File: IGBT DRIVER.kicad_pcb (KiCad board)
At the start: 2 copper layers, 145 x 70 mm, 123 parts, among them J1 Conn_01x04, J2 Conn_01x04, J3 Conn_01x01, J4 Conn_01x04, J5 Conn_02x05_Odd_Even, J6 Conn_01x02_Male, Q1 MMBT5551L, Q2 MMBT5551L, Q3 MMBT5551L, Q4 MMBT5401, Q5 MMBT5551L, Q6 MMBT5551L, Q7 MMBT5551L, Q8 MMBT5551L, U1 miw06-24s24, U2 EXB841, U3 PC817, U4 SN75452BP, U5 AMS1117-5.0, U6 PC817, U7 PC817

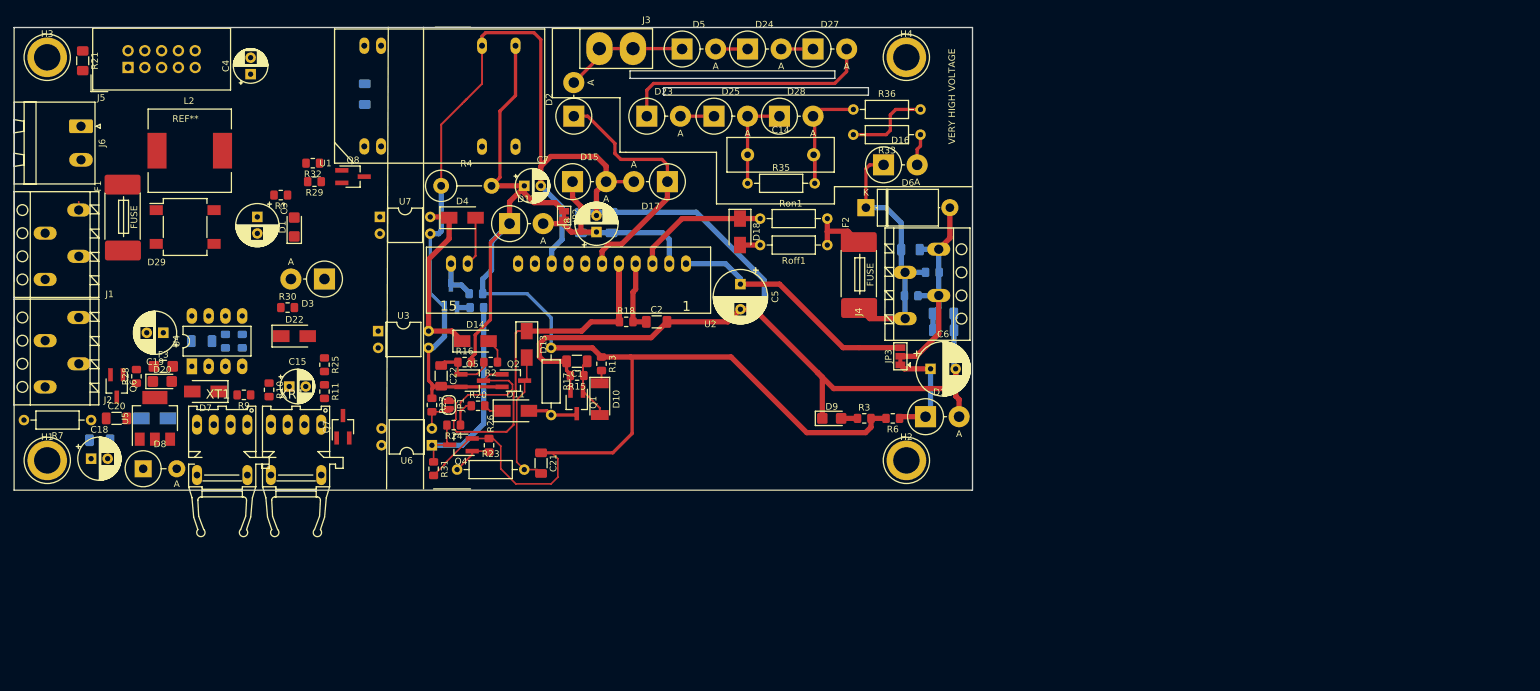
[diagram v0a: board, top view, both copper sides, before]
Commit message: skm200 layout added
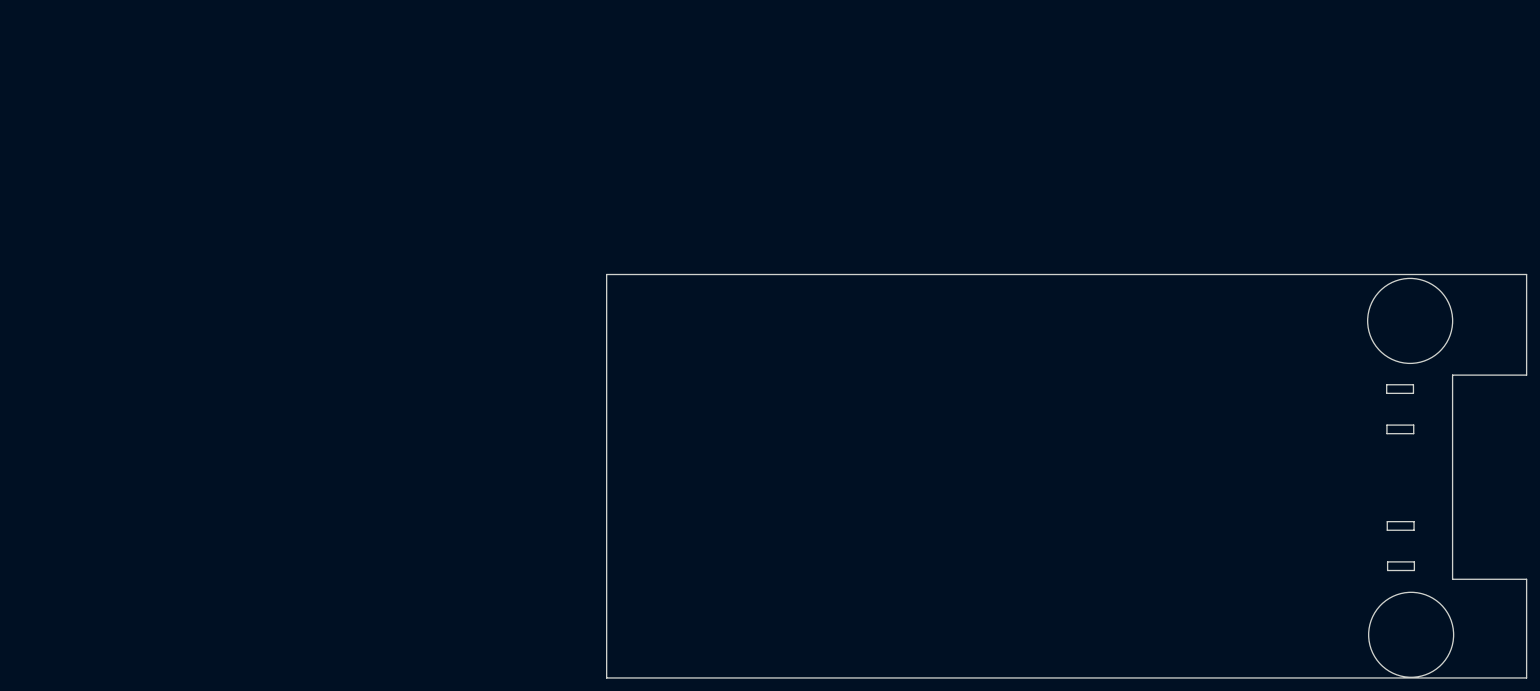
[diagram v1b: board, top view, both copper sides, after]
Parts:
- removed C1: 1nF, Capacitor_SMD:C_1206_3216Metric_Pad1.33x1.80mm_HandSolder
- removed C10, C11: 1uF, Capacitor_SMD:C_1206_3216Metric_Pad1.33x1.80mm_HandSolder
- removed C12, C13, C16, C17, C20: 100nF, Capacitor_SMD:C_1206_3216Metric_Pad1.33x1.80mm_HandSolder
- removed C14: 100nF, Capacitor_THT:C_Disc_D16.0mm_W5.0mm_P10.00mm
- removed C15: 4.7uf/16v, Capacitor_THT:CP_Radial_D5.0mm_P2.50mm
- removed C18, C19, C3, C8: 100uf/35v, Capacitor_THT:CP_Radial_D6.3mm_P2.50mm
- removed C2: C, Capacitor_SMD:C_1206_3216Metric_Pad1.33x1.80mm_HandSolder
- removed C21: 100pF, Capacitor_SMD:C_1206_3216Metric_Pad1.33x1.80mm_HandSolder
- removed C22: 10uF, Capacitor_SMD:C_1206_3216Metric_Pad1.33x1.80mm_HandSolder
- removed C4, C7: 10uf/35v, Capacitor_THT:CP_Radial_D5.0mm_P2.50mm
- removed C5, C6: 47uf/35v, Capacitor_THT:CP_Radial_D8.0mm_P3.80mm
- removed C9: 100nf, Capacitor_SMD:C_1206_3216Metric_Pad1.33x1.80mm_HandSolder
- removed Cclamp1: C, Capacitor_SMD:C_1206_3216Metric
- removed D1, D20, D9: LED, LED_SMD:LED_1206_3216Metric_Castellated
- removed D10: BZX85C20, Diode_SMD:D_MELF
- removed D11, D13, D14, D18, D21, D22, D4: SS14, Diode_SMD:D_SMA
- removed D12, D3: 1.5KE4A, Diode_THT:D_DO-201AD_P5.08mm_Vertical_AnodeUp
- removed D15: 1.5KE24A, Diode_THT:D_DO-201AD_P5.08mm_Vertical_AnodeUp
- removed D16: 1.5KE7A, Diode_THT:D_DO-201AD_P5.08mm_Vertical_AnodeUp
- removed D17: 1.5KE13A, Diode_THT:D_DO-201AD_P5.08mm_Vertical_AnodeUp
- removed D19: 1.5KE8A, Diode_THT:D_DO-201AD_P5.08mm_Vertical_AnodeUp
- removed D2: BYV26E, Diode_THT:D_DO-201AD_P5.08mm_Vertical_AnodeUp
- removed D23, D24, D25, D27, D28, D5: 1.5KE160A, Diode_THT:D_DO-201AD_P5.08mm_Vertical_AnodeUp
- removed D29: DF10M, Diode_SMD:Diode_Bridge_Vishay_DFS
- removed D6: 1.5KE16CA, Diode_THT:D_DO-201AE_P12.70mm_Horizontal
- removed D7: 1N4001, Diode_SMD:D_SMA
- removed D8: 1N5338B, Diode_THT:D_DO-201_P5.08mm_Vertical_AnodeUp
- removed F1, F2: Fuse_Small, gh- kicad:fuse.holder.1808
- removed F3: 0.5A, Fuse:Fuse_1206_3216Metric_Castellated
- removed H1, H2, H3, H4: MountingHole, TestPoint:TestPoint_Plated_Hole_D4.0mm
- removed J1, J2, J4: Conn_01x04, gh- kicad:WJ250-3.5
- removed J3: Conn_01x01, gh- kicad:COOLERI
- removed J5: Conn_02x05_Odd_Even, Connector_IDC:IDC-Header_2x05_P2.54mm_Vertical
- removed J6: Conn_01x02_Male, Connector_Phoenix_MSTB:PhoenixContact_MSTBA_2,5_2-G-5,08_1x02_P5.08mm_Horizontal
- removed JP1: SolderJumper_2_Open, Jumper:SolderJumper-2_P1.3mm_Open_RoundedPad1.0x1.5mm
- removed JP2: SolderJumper_2_Bridged, Jumper:SolderJumper-2_P1.3mm_Bridged_Pad1.0x1.5mm
- removed JP3: SolderJumper_3_Bridged12, Jumper:SolderJumper-3_P1.3mm_Bridged12_Pad1.0x1.5mm
- removed L2: 10uh, gh- kicad:INDUCTOR.SMD.12
- removed Q1, Q2, Q3, Q5, Q6, Q7, Q8: MMBT5551L, Package_TO_SOT_SMD:SOT-23W_Handsoldering
- removed Q4: MMBT5401, Package_TO_SOT_SMD:SOT-23W_Handsoldering
- removed R1, R19, R3: 1.8k, Resistor_SMD:R_0805_2012Metric_Pad1.15x1.40mm_HandSolder
- removed R10, R11: 2.7k, Resistor_SMD:R_0805_2012Metric_Pad1.15x1.40mm_HandSolder
- removed R12, R14, R22, R25, R29, R30, R32, R9: 1k, Resistor_SMD:R_0805_2012Metric_Pad1.15x1.40mm_HandSolder
- removed R13, R15: 1K, Resistor_SMD:R_0805_2012Metric_Pad1.15x1.40mm_HandSolder
- removed R16, R2: r, Resistor_SMD:R_0805_2012Metric_Pad1.15x1.40mm_HandSolder
- removed R17, R23: 3.3k-1/4W, Resistor_THT:R_Axial_DIN0207_L6.3mm_D2.5mm_P10.16mm_Horizontal
- removed R18: R, Resistor_SMD:R_0805_2012Metric_Pad1.15x1.40mm_HandSolder
- removed R20: 500R, Resistor_SMD:R_0805_2012Metric_Pad1.15x1.40mm_HandSolder
- removed R21: 10/0.25W, Resistor_SMD:R_1206_3216Metric_Pad1.42x1.75mm_HandSolder
- removed R24, R26, R27: 3.3K, Resistor_SMD:R_0805_2012Metric_Pad1.15x1.40mm_HandSolder
- removed R28: 10K, Resistor_SMD:R_0805_2012Metric_Pad1.15x1.40mm_HandSolder
- removed R31: not mount, Resistor_SMD:R_0805_2012Metric_Pad1.15x1.40mm_HandSolder
- removed R33: 100, Resistor_THT:R_Axial_DIN0207_L6.3mm_D2.5mm_P10.16mm_Horizontal
- removed R34, R8: 20K, Resistor_SMD:R_0805_2012Metric_Pad1.15x1.40mm_HandSolder
- removed R35: 20K, Resistor_THT:R_Axial_DIN0207_L6.3mm_D2.5mm_P10.16mm_Horizontal
- removed R36: 120, Resistor_THT:R_Axial_DIN0207_L6.3mm_D2.5mm_P10.16mm_Horizontal
- removed R4: 2k/1w, Resistor_THT:R_Axial_DIN0414_L11.9mm_D4.5mm_P7.62mm_Vertical
- removed R5: 3k, Resistor_SMD:R_0805_2012Metric_Pad1.15x1.40mm_HandSolder
- removed R6: 6.8k, Resistor_SMD:R_0805_2012Metric_Pad1.15x1.40mm_HandSolder
- removed R7: 10/0.25W, Resistor_THT:R_Axial_DIN0207_L6.3mm_D2.5mm_P10.16mm_Horizontal
- removed Roff1, Ron1: 20, Resistor_THT:R_Axial_DIN0207_L6.3mm_D2.5mm_P10.16mm_Horizontal
- removed U1: miw06-24s24, gh- kicad:MIWI06
- removed U2: EXB841, gh- kicad:EXB841
- removed U3, U6, U7: PC817, Package_DIP:DIP-4_W7.62mm
- removed U4: SN75452BP, Package_DIP:DIP-8_W7.62mm_LongPads
- removed U5: AMS1117-5.0, Package_TO_SOT_SMD:SOT-223-3_TabPin2
- removed XR1: HFBR-2521, gh- kicad:HFBR-15X3
- removed XT1: HFBR-1521, KIcad:HFBR-15X3
- added G***: LOGO, IGBT-DRIVER-emad:skm200GB, F.Cu at (342.3, 121.9)
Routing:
- net GNDPWR: track 296.7 -> 0.00 mm
- net +24V: track 211.1 -> 0.00 mm
- net /Fault: track 62.9 -> 0.00 mm
- net VPP: track 44.2 -> 0.00 mm
- net /GATE: track 40.6 -> 0.00 mm
- net Net-(D23-Pad1): track 38.7 -> 0.00 mm
- net /EMITTER: track 38.7 -> 0.00 mm
- net Net-(D17-Pad1): track 38.3 -> 0.00 mm
- net Net-(C5-Pad1): track 38.2 -> 0.00 mm
- net /lockpwm: track 35.3 -> 0.00 mm
- net /Latchreset: track 27.1 -> 0.00 mm
- net Net-(Q2-Pad1): track 24.7 -> 0.00 mm
- net Net-(C14-Pad2): track 21.2 -> 0.00 mm
- net Net-(C21-Pad2): track 20.8 -> 0.00 mm
- net Net-(D18-Pad1): track 20.5 -> 0.00 mm
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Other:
- board size 145 x 70 mm -> 139.2 x 61 mm
- board text removed: "VERY HIGH VOLTAGE"

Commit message: skm200 3d
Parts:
- removed G***: LOGO, IGBT-DRIVER-emad:skm200GB
- added C1: 100nF, Capacitor_SMD:C_1206_3216Metric_Pad1.33x1.80mm_HandSolder, F.Cu at (315.7, 39.5)
- added C10: 47uf/35v, Capacitor_THT:CP_Radial_D8.0mm_P3.80mm, F.Cu at (332.2, 69.8)
- added C11: 1uF, Capacitor_SMD:C_1206_3216Metric_Pad1.33x1.80mm_HandSolder, F.Cu at (396.3, 3.49)
- added C12: 100nF, Capacitor_THT:C_Disc_D16.0mm_W5.0mm_P10.00mm, F.Cu at (277.2, 48.0)
- added C13: 100nF, Capacitor_SMD:C_1206_3216Metric_Pad1.33x1.80mm_HandSolder, F.Cu at (396.3, 6.84)
- added C14: 10nF, Capacitor_SMD:C_1206_3216Metric_Pad1.33x1.80mm_HandSolder, F.Cu at (327.5, 84.5)
- added C15: 1nF, Capacitor_SMD:C_1206_3216Metric_Pad1.33x1.80mm_HandSolder, F.Cu at (341.9, 67.8)
- added C16: 10uf/35v, Capacitor_THT:CP_Radial_D5.0mm_P2.50mm, F.Cu at (388.8, 5.59)
- added C17: 100nf, Capacitor_SMD:C_1206_3216Metric_Pad1.33x1.80mm_HandSolder, F.Cu at (389.8, 13.9)
- added C18: 10uf/35v, Capacitor_THT:CP_Radial_D5.0mm_P2.50mm, F.Cu at (393.1, -1.46)
- added C19: 1uF, Capacitor_SMD:C_1206_3216Metric_Pad1.33x1.80mm_HandSolder, F.Cu at (383.7, 17.2)
- added C2: 47uf/35v, Capacitor_THT:CP_Radial_D8.0mm_P3.80mm, F.Cu at (332.2, 20.3)
- added C20: 100nF, Capacitor_SMD:C_1206_3216Metric_Pad1.33x1.80mm_HandSolder, F.Cu at (383.1, 21.3)
- added C21: 47uf/35v, Capacitor_THT:CP_Radial_D8.0mm_P3.80mm, F.Cu at (322.3, 28.5)
- added C22: 100nF, Capacitor_SMD:C_1206_3216Metric_Pad1.33x1.80mm_HandSolder, F.Cu at (327.5, 35.0)
- added C23: 47uf/35v, Capacitor_THT:CP_Radial_D8.0mm_P3.80mm, F.Cu at (322.3, 78.0)
- added C24: 100nF, Capacitor_SMD:C_1206_3216Metric_Pad1.33x1.80mm_HandSolder, F.Cu at (303.7, 88.6)
- added C3: 100uf/35v, Capacitor_THT:CP_Radial_D6.3mm_P2.50mm, F.Cu at (361.9, 11.3)
- added C4: 10uf/35v, Capacitor_THT:CP_Radial_D5.0mm_P2.50mm, F.Cu at (376.2, 16.3)
- added C5: 1nF, Capacitor_SMD:C_1206_3216Metric_Pad1.33x1.80mm_HandSolder, F.Cu at (341.9, 15.0)
- added C6: 100nF, Capacitor_SMD:C_1206_3216Metric_Pad1.33x1.80mm_HandSolder, F.Cu at (346.1, 61.1)
- added C7: 10uf/35v, Capacitor_THT:CP_Radial_D5.0mm_P2.50mm, F.Cu at (399.8, -1.46)
- added C8: 100uf/35v, Capacitor_THT:CP_Radial_D6.3mm_P2.50mm, F.Cu at (374.5, 9.14)
- added C9: 100nf, Capacitor_SMD:C_1206_3216Metric_Pad1.33x1.80mm_HandSolder, F.Cu at (389.7, 10.5)
- added CDynamic1: 100nF, Capacitor_THT:C_Disc_D16.0mm_W5.0mm_P10.00mm, F.Cu at (277.2, -1.46)
- added CShortPulseFilter1: 100pF, Capacitor_SMD:C_1206_3216Metric_Pad1.33x1.80mm_HandSolder, F.Cu at (303.7, 39.1)
- added CblankTime1: 100pF, Capacitor_SMD:C_1206_3216Metric_Pad1.33x1.80mm_HandSolder, F.Cu at (346.1, 11.6)
- added Cclamp1: C, Capacitor_SMD:C_1206_3216Metric, F.Cu at (316.0, 14.5)
- added Cclamp2: C, Capacitor_SMD:C_1206_3216Metric, F.Cu at (316.0, 64.0)
- added Cex1: 96pF, Capacitor_SMD:C_1206_3216Metric_Pad1.33x1.80mm_HandSolder, F.Cu at (309.7, 39.1)
- added Cex2: 1nF, Capacitor_SMD:C_1206_3216Metric_Pad1.33x1.80mm_HandSolder, F.Cu at (348.9, 8.24)
- added Cex3: 96pF, Capacitor_SMD:C_1206_3216Metric_Pad1.33x1.80mm_HandSolder, F.Cu at (309.7, 88.6)
- added Cex4: 100pF, Capacitor_SMD:C_1206_3216Metric_Pad1.33x1.80mm_HandSolder, F.Cu at (315.7, 89.0)
- added Cex5: 100pF, Capacitor_SMD:C_1206_3216Metric_Pad1.33x1.80mm_HandSolder, F.Cu at (341.9, 64.5)
- added Cex6: 1nF, Capacitor_SMD:C_1206_3216Metric_Pad1.33x1.80mm_HandSolder, F.Cu at (332.0, 76.2)
- added Cex7: 22nF, Capacitor_SMD:C_1206_3216Metric_Pad1.33x1.80mm_HandSolder, F.Cu at (348.9, 57.7)
- added CsoftTurnOff2: 10nF, Capacitor_SMD:C_1206_3216Metric_Pad1.33x1.80mm_HandSolder, F.Cu at (332.0, 26.7)
- added CsoftTurnOffTiming1: 22nF, Capacitor_SMD:C_1206_3216Metric_Pad1.33x1.80mm_HandSolder, F.Cu at (341.9, 18.3)
- added D1: LED, LED_SMD:LED_1206_3216Metric_Castellated, F.Cu at (383.8, 13.9)
- added D10: Dz8v, Diode_THT:D_DO-201AD_P5.08mm_Vertical_AnodeUp, F.Cu at (311.8, 78.8)
- added D11: 1.5KE13A, Diode_THT:D_DO-201AD_P5.08mm_Vertical_AnodeUp, F.Cu at (345.1, 48.1)
- added D12: 1.5KE6V8A, Diode_THT:D_DO-201AD_P5.08mm_Vertical_AnodeUp, F.Cu at (327.6, 61.6)
- added D13: BYV26E, Diode_THT:D_DO-201AD_P5.08mm_Vertical_AnodeUp, F.Cu at (290.1, 83.5)
- added D14: Dz10v, Diode_THT:D_DO-201AD_P5.08mm_Vertical_AnodeUp, F.Cu at (311.8, 72.0)
- added D15: 26v TVS, Diode_SMD:D_MELF, F.Cu at (296.8, 89.1)
- added D16: 1.5KE160A, Diode_THT:D_DO-201AD_P5.08mm_Vertical_AnodeUp, F.Cu at (327.6, 54.9)
- added D17: 1.5KE160A, Diode_THT:D_DO-201AD_P5.08mm_Vertical_AnodeUp, F.Cu at (301.0, 76.8)
- added D18: 1.5KE160A, Diode_THT:D_DO-201AD_P5.08mm_Vertical_AnodeUp, F.Cu at (338.4, 54.9)
- added D19: 1.5KE160A, Diode_THT:D_DO-201AD_P5.08mm_Vertical_AnodeUp, F.Cu at (301.0, 83.6)
- added D2: 1.5KE4A, Diode_THT:D_DO-201AD_P5.08mm_Vertical_AnodeUp, F.Cu at (338.4, 5.39)
- added D20: 1.5KE160A, Diode_THT:D_DO-201AD_P5.08mm_Vertical_AnodeUp, F.Cu at (316.7, 52.2)
- added D21: 1.5KE160A, Diode_THT:D_DO-201AD_P5.08mm_Vertical_AnodeUp, F.Cu at (334.3, 48.1)
- added D22: BZX85C20, Diode_SMD:D_MELF, F.Cu at (288.9, 89.0)
- added D29: DF10M, Diode_SMD:Diode_Bridge_Vishay_DFS, F.Cu at (377.8, 0.24)
- added D3: Dz8v, Diode_THT:D_DO-201AD_P5.08mm_Vertical_AnodeUp, F.Cu at (316.7, 2.69)
- added D4: 1.5KE13A, Diode_THT:D_DO-201AD_P5.08mm_Vertical_AnodeUp, F.Cu at (301.0, 27.3)
- added D5: BYV26E, Diode_THT:D_DO-201AD_P5.08mm_Vertical_AnodeUp, F.Cu at (316.7, 9.44)
- added D6: 1.5KE6V8A, Diode_THT:D_DO-201AD_P5.08mm_Vertical_AnodeUp, F.Cu at (334.3, -1.36)
- added D7: 26v TVS, Diode_SMD:D_MELF, F.Cu at (296.8, 39.6)
- added D8: 1.5KE4A, Diode_THT:D_DO-201AD_P5.08mm_Vertical_AnodeUp, F.Cu at (316.7, 58.9)
- added D9: LED, LED_SMD:LED_1206_3216Metric_Castellated, F.Cu at (377.1, 21.3)
- added DStatic1: 1.5KE160A, Diode_THT:D_DO-201AD_P5.08mm_Vertical_AnodeUp, F.Cu at (327.6, 5.39)
- added DStatic2: 1.5KE160A, Diode_THT:D_DO-201AD_P5.08mm_Vertical_AnodeUp, F.Cu at (311.8, 22.5)
- added DStatic3: 1.5KE160A, Diode_THT:D_DO-201AD_P5.08mm_Vertical_AnodeUp, F.Cu at (301.0, 34.1)
- added DStatic4: 1.5KE160A, Diode_THT:D_DO-201AD_P5.08mm_Vertical_AnodeUp, F.Cu at (290.1, 34.0)
- added DStatic5: 1.5KE160A, Diode_THT:D_DO-201AD_P5.08mm_Vertical_AnodeUp, F.Cu at (345.1, -1.36)
- added DZunderVoltageFault1: BZX85C20, Diode_SMD:D_MELF, F.Cu at (288.9, 39.5)
- added Dex1: 1n4148, Diode_SMD:D_SMA, F.Cu at (339.1, 11.0)
- added Dex10: 1n4148, Diode_SMD:D_SMA, F.Cu at (312.4, 84.4)
- added Dex2: 1n4148, Diode_SMD:D_SMA, F.Cu at (312.4, 34.9)
- added Dex3: 1n4148, Diode_SMD:D_SMA, F.Cu at (320.5, 85.1)
- added Dex4: 1n4148, Diode_SMD:D_SMA, F.Cu at (302.3, 70.9)
- added Dex5: 1n4148, Diode_SMD:D_SMA, F.Cu at (320.5, 35.6)
- added Dex6: 1n4148, Diode_SMD:D_SMA, F.Cu at (349.9, 53.8)
- added Dex7: 1n4148, Diode_SMD:D_SMA, F.Cu at (339.1, 60.5)
- added DprotectionHigh1: 1n4148, Diode_SMD:D_SMA, F.Cu at (302.3, 21.4)
- added DprotectionLow1: 1n4148, Diode_SMD:D_SMA, F.Cu at (349.9, 4.29)
- added DzDynamic1: 1.5KE160A, Diode_THT:D_DO-201AD_P5.08mm_Vertical_AnodeUp, F.Cu at (311.8, 29.3)
- added DzSaturation1: Dz10v, Diode_THT:D_DO-201AD_P5.08mm_Vertical_AnodeUp, F.Cu at (327.6, 12.1)
- added H1: MountingHole, TestPoint:TestPoint_Plated_Hole_D4.0mm, F.Cu at (370.6, 16.6)
- added H2: MountingHole, TestPoint:TestPoint_Plated_Hole_D4.0mm, F.Cu at (362.6, 18.7)
- added H3: MountingHole, TestPoint:TestPoint_Plated_Hole_D4.0mm, F.Cu at (383.2, 8.74)
- added H4: MountingHole, TestPoint:TestPoint_Plated_Hole_D4.0mm, F.Cu at (387.5, -1.21)
- added Q1: BC817, Package_TO_SOT_SMD:SOT-23, F.Cu at (351.5, 12.2)
- added Q10: BC817, Package_TO_SOT_SMD:SOT-23, F.Cu at (337.2, 81.4)
- added Q11: BC817, Package_TO_SOT_SMD:SOT-23, F.Cu at (351.5, 61.7)
- added Q12: BC817, Package_TO_SOT_SMD:SOT-23, F.Cu at (345.5, 71.8)
- added Q13: BC817, Package_TO_SOT_SMD:SOT-23, F.Cu at (332.7, 84.7)
- added Q14: BC807, Package_TO_SOT_SMD:SOT-23, F.Cu at (326.7, 88.4)
- added Q15: BC817, Package_TO_SOT_SMD:SOT-23, F.Cu at (341.1, 71.8)
- added Q16: BC817, Package_TO_SOT_SMD:SOT-23, F.Cu at (337.2, 76.8)
- added Q17: BC807, Package_TO_SOT_SMD:SOT-23, F.Cu at (347.1, 65.0)
- added Q18: BC817, Package_TO_SOT_SMD:SOT-23, F.Cu at (331.2, 80.2)
- added Q19: TIP41, Package_TO_SOT_THT:TO-220-3_Vertical, F.Cu at (290.0, 71.4)
- added Q2: BC817, Package_TO_SOT_SMD:SOT-23, F.Cu at (345.5, 22.3)
- added Q20: TIP42, Package_TO_SOT_THT:TO-220-3_Vertical, F.Cu at (276.7, 87.6)
- added Q3: BC817, Package_TO_SOT_SMD:SOT-23, F.Cu at (337.2, 31.9)
- added Q4: BC807, Package_TO_SOT_SMD:SOT-23, F.Cu at (332.7, 35.2)
- added Q5: BC817, Package_TO_SOT_SMD:SOT-23, F.Cu at (326.7, 38.9)
- added Q6: BC817, Package_TO_SOT_SMD:SOT-23, F.Cu at (341.1, 22.3)
- added Q7: BC817, Package_TO_SOT_SMD:SOT-23, F.Cu at (337.2, 27.3)
- added Q8: TIP41, Package_TO_SOT_THT:TO-220-3_Vertical, F.Cu at (276.7, 38.1)
- added Q9: TIP42, Package_TO_SOT_THT:TO-220-3_Vertical, F.Cu at (290.0, 21.9)
- added Qclamp1: BUK7880-55A, Package_TO_SOT_SMD:SOT-223-3_TabPin2, F.Cu at (324.2, 19.6)
- added Qclamp2: BUK7880-55A, Package_TO_SOT_SMD:SOT-223-3_TabPin2, F.Cu at (324.2, 69.1)
- added QfaultLatch1: BC807, Package_TO_SOT_SMD:SOT-23, F.Cu at (331.2, 30.7)
- added QsoftTurnOnn1: BC817, Package_TO_SOT_SMD:SOT-23, F.Cu at (347.1, 15.5)
- added R10: 2k/1w, Resistor_THT:R_Axial_DIN0414_L11.9mm_D4.5mm_P7.62mm_Vertical, F.Cu at (362.1, -1.71)
- added R14: 20K, Resistor_THT:R_Axial_DIN0207_L6.3mm_D2.5mm_P10.16mm_Horizontal, F.Cu at (301.6, 54.9)
- added R15: 10, Resistor_THT:R_Axial_DIN0207_L6.3mm_D2.5mm_P10.16mm_Horizontal, F.Cu at (288.3, 65.5)
- added R16: 3.3k-1/4W, Resistor_THT:R_Axial_DIN0207_L6.3mm_D2.5mm_P10.16mm_Horizontal, F.Cu at (288.3, 61.4)
- added R17: 220, Resistor_THT:R_Axial_DIN0207_L6.3mm_D2.5mm_P10.16mm_Horizontal, F.Cu at (319.2, 46.8)
- added R4: 2k/1w, Resistor_THT:R_Axial_DIN0414_L11.9mm_D4.5mm_P7.62mm_Vertical, F.Cu at (362.1, 4.34)
- added R6: 3.3k-1/4W, Resistor_THT:R_Axial_DIN0207_L6.3mm_D2.5mm_P10.16mm_Horizontal, F.Cu at (275.0, 20.0)
- added R7: 220, Resistor_THT:R_Axial_DIN0207_L6.3mm_D2.5mm_P10.16mm_Horizontal, F.Cu at (288.3, 11.9)
- added RAfterfaultTurnOnDelay1: 2.2k, Resistor_THT:R_Axial_DIN0207_L6.3mm_D2.5mm_P10.16mm_Horizontal, F.Cu at (275.0, 28.1)
- added RBlankTime1: 2.2k, Resistor_THT:R_Axial_DIN0207_L6.3mm_D2.5mm_P10.16mm_Horizontal, F.Cu at (301.6, 1.34)
- added RDynamic1: 20K, Resistor_THT:R_Axial_DIN0207_L6.3mm_D2.5mm_P10.16mm_Horizontal, F.Cu at (275.0, 24.1)
- added RSofTurnoffTiming1: 1k, Resistor_THT:R_Axial_DIN0207_L6.3mm_D2.5mm_P10.16mm_Horizontal, F.Cu at (288.3, 16.0)
- added Rex1: 6.8k, Resistor_THT:R_Axial_DIN0207_L6.3mm_D2.5mm_P10.16mm_Horizontal, F.Cu at (275.0, 3.84)
- added Rex10: 56k, Resistor_THT:R_Axial_DIN0207_L6.3mm_D2.5mm_P10.16mm_Horizontal, F.Cu at (301.6, 50.8)
- added Rex11: 2.2k, Resistor_THT:R_Axial_DIN0207_L6.3mm_D2.5mm_P10.16mm_Horizontal, F.Cu at (275.0, 57.4)
- added Rex12: 2.2k, Resistor_THT:R_Axial_DIN0207_L6.3mm_D2.5mm_P10.16mm_Horizontal, F.Cu at (288.3, 53.3)
- added Rex13: 220, Resistor_THT:R_Axial_DIN0207_L6.3mm_D2.5mm_P10.16mm_Horizontal, F.Cu at (275.0, 61.4)
- added Rex14: 1k, Resistor_THT:R_Axial_DIN0207_L6.3mm_D2.5mm_P10.16mm_Horizontal, F.Cu at (275.0, 65.5)
- added Rex15: 1k, Resistor_THT:R_Axial_DIN0207_L6.3mm_D2.5mm_P10.16mm_Horizontal, F.Cu at (305.9, 46.8)
- added Rex16: 2.2k, Resistor_THT:R_Axial_DIN0207_L6.3mm_D2.5mm_P10.16mm_Horizontal, F.Cu at (275.0, 69.5)
- added Rex17: 2.2k, Resistor_THT:R_Axial_DIN0207_L6.3mm_D2.5mm_P10.16mm_Horizontal, F.Cu at (288.3, 57.4)
- added Rex18: 1k, Resistor_THT:R_Axial_DIN0207_L6.3mm_D2.5mm_P10.16mm_Horizontal, F.Cu at (275.0, 73.6)
- added Rex2: 56k, Resistor_THT:R_Axial_DIN0207_L6.3mm_D2.5mm_P10.16mm_Horizontal, F.Cu at (288.3, 7.89)
- added Rex3: 2.2k, Resistor_THT:R_Axial_DIN0207_L6.3mm_D2.5mm_P10.16mm_Horizontal, F.Cu at (292.6, -2.71)
- added Rex4: 220, Resistor_THT:R_Axial_DIN0207_L6.3mm_D2.5mm_P10.16mm_Horizontal, F.Cu at (305.9, -2.71)
- added Rex5: 1k, Resistor_THT:R_Axial_DIN0207_L6.3mm_D2.5mm_P10.16mm_Horizontal, F.Cu at (275.0, 16.0)
- added Rex6: 2.2k, Resistor_THT:R_Axial_DIN0207_L6.3mm_D2.5mm_P10.16mm_Horizontal, F.Cu at (275.0, 11.9)
- added Rex7: 1k, Resistor_THT:R_Axial_DIN0207_L6.3mm_D2.5mm_P10.16mm_Horizontal, F.Cu at (288.3, 3.84)
- added Rex8: 6.8k, Resistor_THT:R_Axial_DIN0207_L6.3mm_D2.5mm_P10.16mm_Horizontal, F.Cu at (275.0, 81.7)
- added Rex9: 120, Resistor_THT:R_Axial_DIN0207_L6.3mm_D2.5mm_P10.16mm_Horizontal, F.Cu at (292.6, 46.8)
- added Roff1: 20, Resistor_THT:R_Axial_DIN0207_L6.3mm_D2.5mm_P10.16mm_Horizontal, F.Cu at (275.0, 7.89)
- added Roff2: 20, Resistor_THT:R_Axial_DIN0207_L6.3mm_D2.5mm_P10.16mm_Horizontal, F.Cu at (275.0, 77.6)
- added Ron1: 20, Resistor_THT:R_Axial_DIN0207_L6.3mm_D2.5mm_P10.16mm_Horizontal, F.Cu at (319.2, -2.71)
- added Ron2: 20, Resistor_THT:R_Axial_DIN0207_L6.3mm_D2.5mm_P10.16mm_Horizontal, F.Cu at (275.0, 53.3)
- added RshortPulseFilter1: 120, Resistor_THT:R_Axial_DIN0207_L6.3mm_D2.5mm_P10.16mm_Horizontal, F.Cu at (301.6, 5.39)
- added RsoftTurnoff2: 10, Resistor_THT:R_Axial_DIN0207_L6.3mm_D2.5mm_P10.16mm_Horizontal, F.Cu at (275.0, 32.2)
- added SYM1: SYM_Arrow45_Normal, IGBT-DRIVER-emad:skm200GB, F.Cu at (342.4, 121.9)
- added U2: 6N136S, Package_DIP:SMDIP-8_W9.53mm, F.Cu at (306.6, 13.3)
- added U3: PC817, Package_DIP:DIP-4_W7.62mm, F.Cu at (288.4, 26.0)
- added U4: 6N136S, Package_DIP:SMDIP-8_W9.53mm, F.Cu at (306.6, 62.8)
- added U5: PC817, Package_DIP:DIP-4_W7.62mm, F.Cu at (288.4, 75.5)
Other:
- outline, holes or cut-outs redrawn

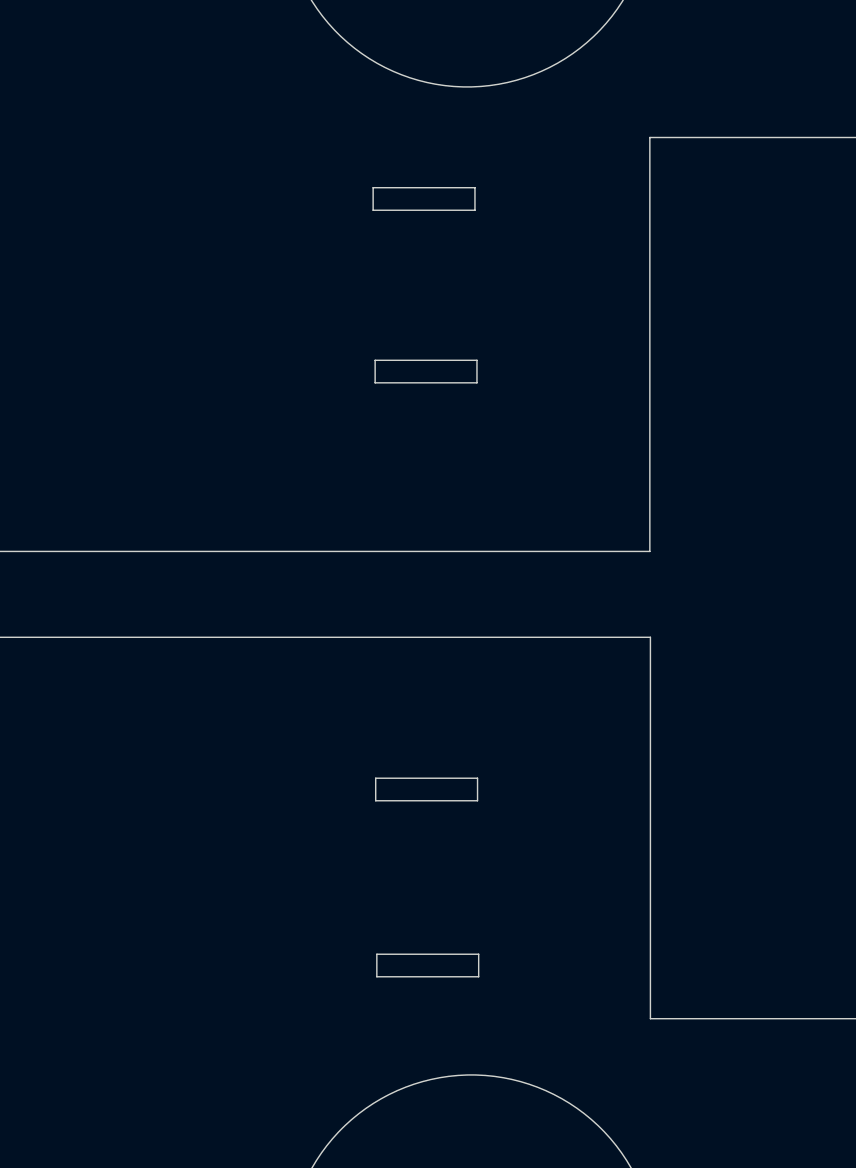
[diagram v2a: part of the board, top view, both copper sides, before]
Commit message: changed bjt
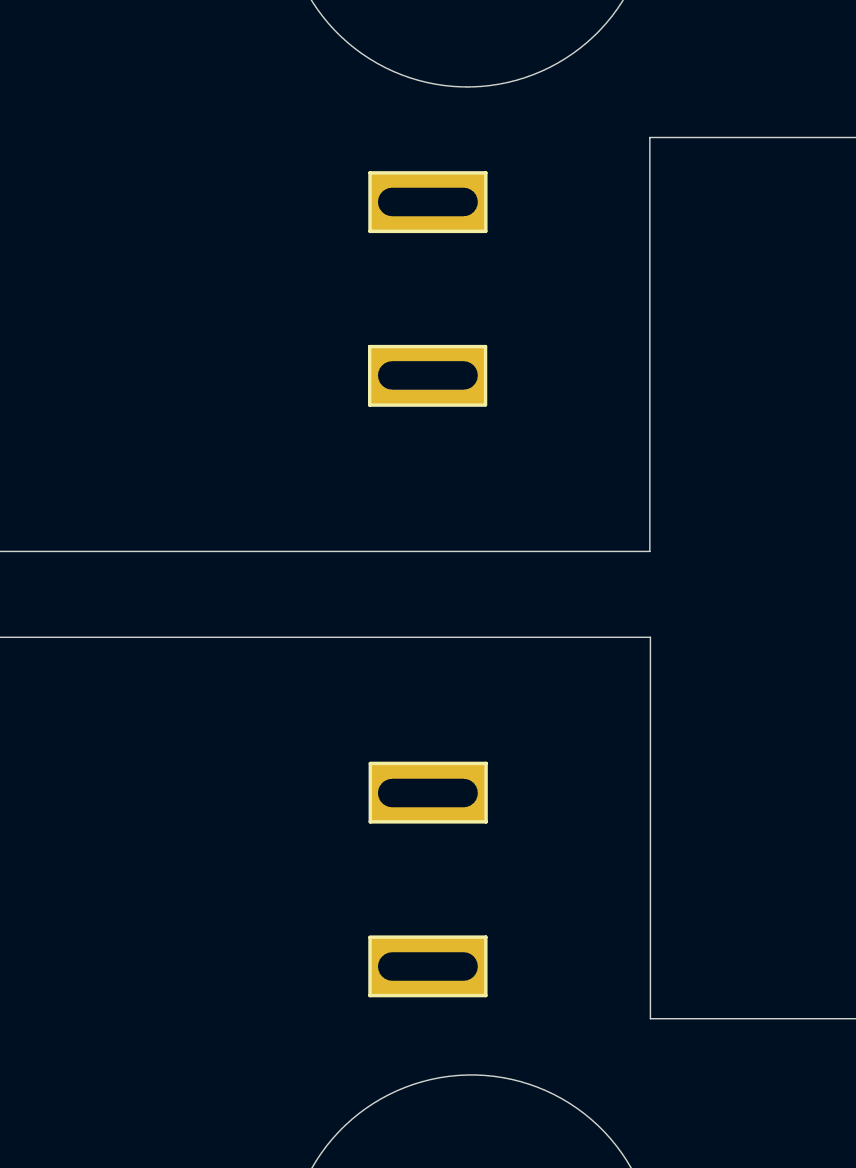
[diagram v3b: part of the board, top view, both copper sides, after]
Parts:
- removed SYM1: SYM_Arrow45_Normal, IGBT-DRIVER-emad:skm200GB
- added IGBTSymbol1: SYM_Arrow45_Normal, IGBT-DRIVER-emad:skm200GB, F.Cu at (342.3, 122.0)
- added J6: Conn_01x02, IGBT-DRIVER-emad:IGBT_Socket, F.Cu at (293.7, 111.8)
- added J7: Conn_01x02, IGBT-DRIVER-emad:IGBT_Socket, F.Cu at (293.7, 132.0)
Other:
- outline, holes or cut-outs redrawn
